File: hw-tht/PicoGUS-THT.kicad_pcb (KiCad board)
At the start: 2 copper layers, 103.7 x 99.8 mm, 82 parts, among them J1 IRQDMA_JP, J3 Bus_ISA_8bit, J5 SJ1-3535NG, J6 UART_TX, J7 USB power jumper, J8 SJ1-3535NG-GR, J9 Waveblaster, U1 Pico, U10 74AHCT126, U11 NE5532, U2 74AHC244, U3 SN74CB3T3257, U4 SN74CB3T3257, U5 74AHC14, U6 74AHC00, U7 74AHC00, U8 APS6404L-3SQR-SN, U9 PCM5100A

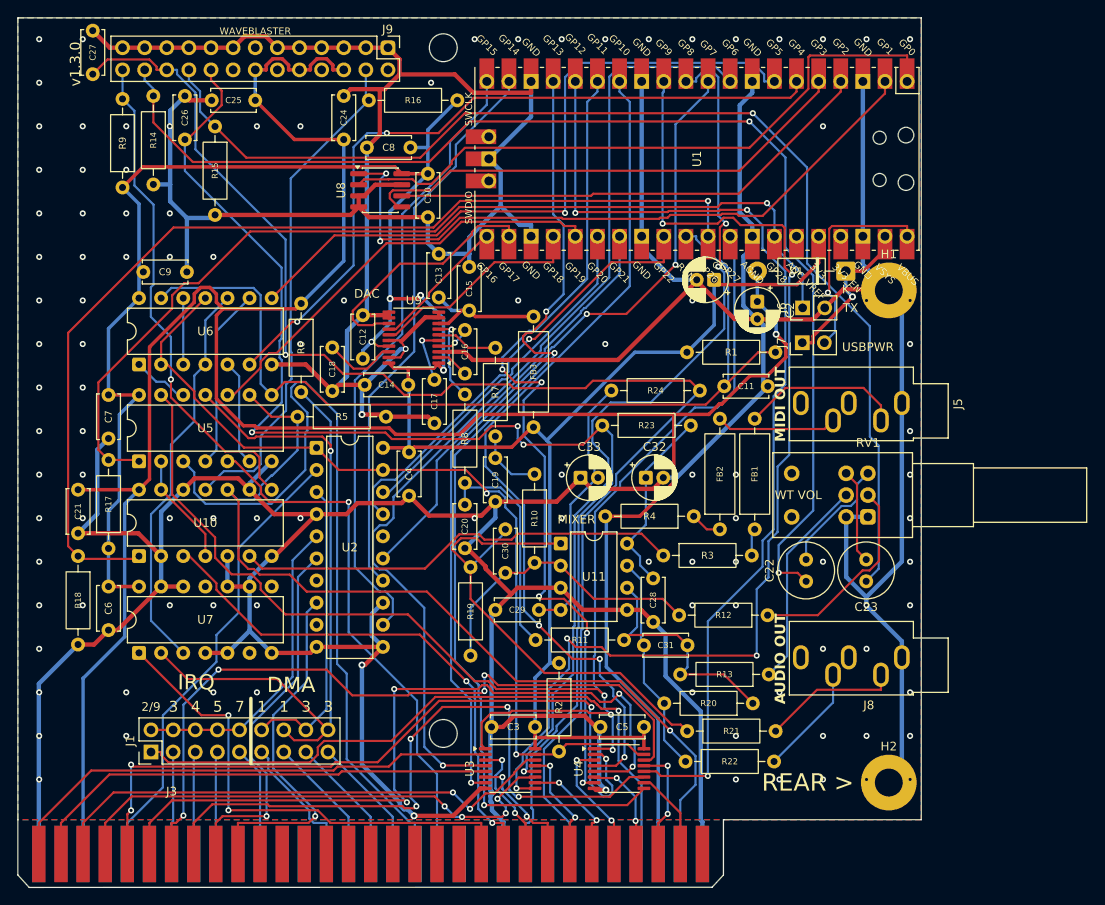
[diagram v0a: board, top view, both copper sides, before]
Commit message: hw-tht: adopt the new hand-made component placement; label clean-up
- THT board rebuilt on the uploaded layout: every part position,
  rotation and reference label kept as placed (R17 moved 0.5 mm down to
  clear C7's courtyard), texts/logo kept; fully re-routed, GND stitched,
  0 DRC errors, 0 unconnected, schematic parity OK. No schematic change
  needed: every cap/resistor sits at the pins it serves.
- Pico pin-name / SWD silkscreen texts removed (THT and SMD).
- WAVEBLASTER, DAC, MIXER and WT VOL labels in Futura bold; WT VOL now
  sits beside RV1 exactly as MIDI OUT / AUDIO OUT sit beside their jacks.
- hw-smd: same label treatment; C23 moved 1.8 mm left to clear WT VOL,
  board re-routed (0 DRC errors).

Co-Authored-By: Claude Opus 5.5 <noreply@anthropic.com>
Claude-Session: https://claude.ai/code/session_011utN3x8yYUNDvkpGCEq5yD
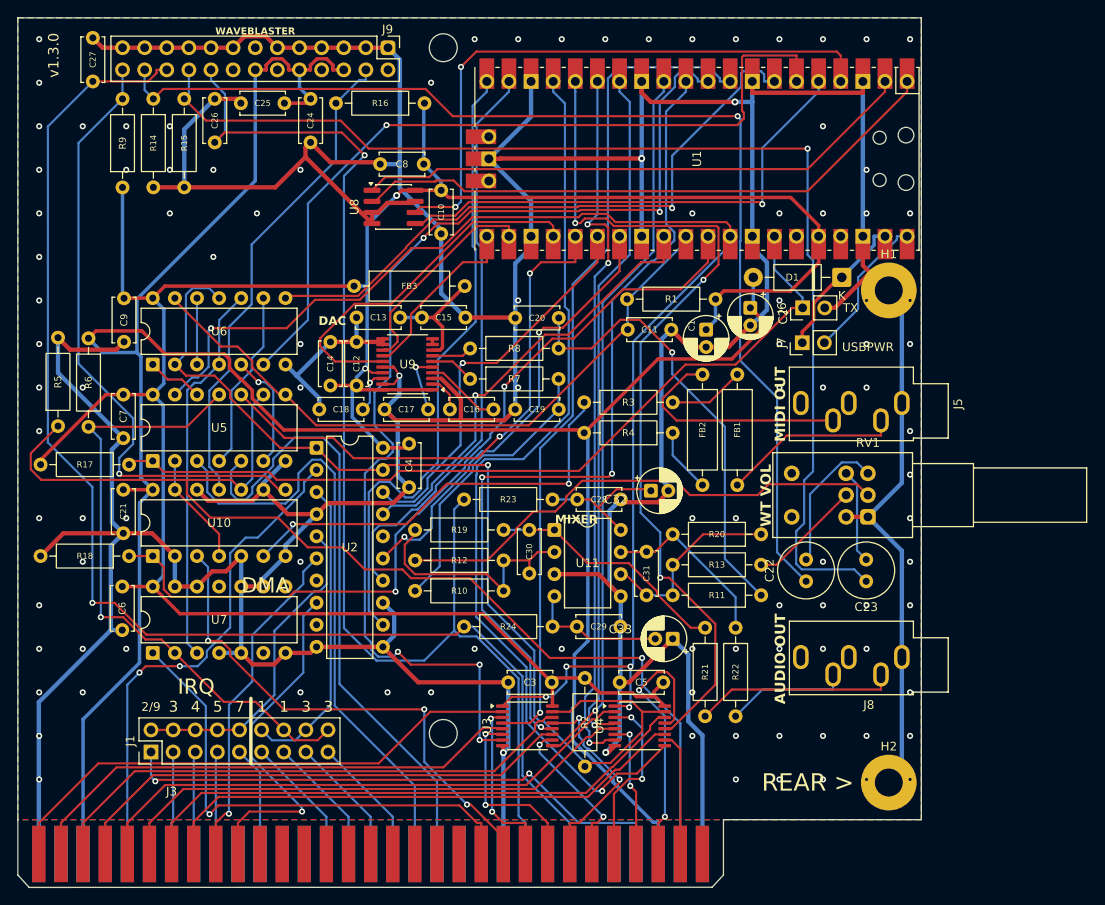
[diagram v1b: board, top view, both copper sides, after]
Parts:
- moved R12 41.0 mm to (162.0, 98.5), turned to 0 degrees
- moved R24 38.3 mm to (167.6, 106.1), turned to 0 degrees
- moved R5 27.5 mm to (121.0, 83.1), turned to 90 degrees
- moved C20 27.1 mm to (173.5, 70.7), turned to 0 degrees
- moved R11 26.4 mm to (201.7, 102.5), turned to 180 degrees
- moved FB3 26.2 mm to (155.0, 67.0), turned to 0 degrees
- moved R6 24.7 mm to (124.5, 73.0)
- moved C33 21.3 mm to (191.6, 107.5), turned to 180 degrees
- moved R3 19.8 mm to (181.4, 80.3)
- moved R20 19.4 mm to (201.7, 95.5)
- moved R10 19.2 mm to (162.0, 102.0), turned to 0 degrees
- moved R23 18.0 mm to (167.6, 91.5)
- moved FB1 17.9 mm to (199.0, 77.2), turned to -90 degrees
- moved R22 16.4 mm to (198.8, 106.2), turned to -90 degrees
- moved R19 15.8 mm to (162.0, 95.0), turned to 0 degrees
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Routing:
- net GND: track 830.6 -> 776.8 mm, vias 109 -> 105
- net AD3: track 126.9 -> 82.1 mm, vias 5 -> 1
- net Net-(R12-Pad1): track 23.5 -> 57.9 mm
- net RUN: track 106.6 -> 77.1 mm
- net Net-(C30-Pad2): track 57.2 -> 28.0 mm
- net AD1: track 98.1 -> 127.0 mm, vias 3 -> 5
- net A5: track 89.0 -> 61.5 mm, vias 4 -> 0
- net /PCM5100 audio/AUDIO_R: track 25.8 -> 51.6 mm, vias 0 -> 1
- net /PCM5100 audio/AUDIO_L: track 7.77 -> 33.2 mm
- net RESET: track 104.0 -> 129.4 mm
- net ~{RI/OCHRDY}: track 117.2 -> 95.5 mm, vias 1 -> 2
- net ~{IOR}: track 90.9 -> 70.6 mm
- net A4: track 84.8 -> 64.8 mm, vias 4 -> 0
- net A6: track 84.6 -> 65.5 mm, vias 4 -> 0
- net AD4: track 97.3 -> 79.0 mm, vias 3 -> 1
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
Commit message: Experimental 2nd IRQ (J10/J11), DMA label fix, labels grouped
- U2's spare channel (2A2 pin 13 -> 2Y2 pin 7, same drive and ~BUSOE as the
  IRQ output) now drives an optional second IRQ: J10 (next to the PSRAM,
  short stub on the fast SPI line) links GPIO3/SPI_TX to 2A2, R25 (10k)
  holds it low when open; J11 (next to J1) links 2Y2 to ISA IRQ3.
  GPIO3 is the PSRAM SPI_TX (all 26 Pico GPIOs are used), so this is for
  firmware that leaves the PSRAM idle. THT and SMD, ERC 0 errors.
- DMA heading moved back beside IRQ above J1.
- Silkscreen labels are members of their circuit-block KiCad groups
  (DAC, MIXER, AUDIO OUT, WT VOL, WAVEBLASTER, MIDI OUT, TX/USBPWR,
  IRQ/DMA + jumper numbers + divider, 2ND IRQ).
- Both boards re-routed: 0 DRC errors, 0 unconnected, schematic parity OK.
- BOMs: R25, J10/J11 (from the 1x40 strip), 6 jumper shunts.

Co-Authored-By: Claude Opus 5.5 <noreply@anthropic.com>
Claude-Session: https://claude.ai/code/session_011utN3x8yYUNDvkpGCEq5yD
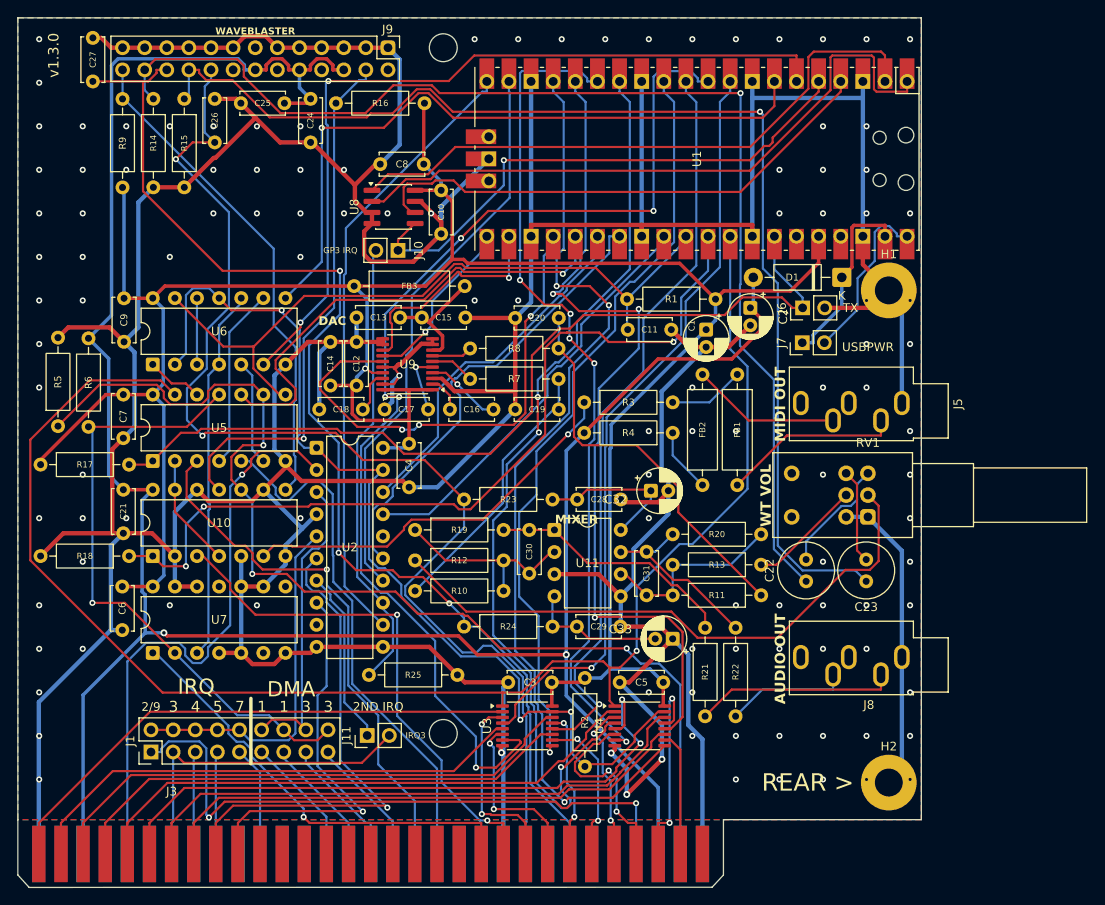
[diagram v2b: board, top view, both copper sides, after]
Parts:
- added J10: Jumper, Connector_PinHeader_2.54mm:PinHeader_1x02_P2.54mm_Vertical, F.Cu at (160.0, 62.9)
- added J11: Jumper, Connector_PinHeader_2.54mm:PinHeader_1x02_P2.54mm_Vertical, F.Cu at (156.5, 118.6)
- added R25: 10K, Resistor_THT:R_Axial_DIN0207_L6.3mm_D2.5mm_P10.16mm_Horizontal, F.Cu at (156.7, 111.7)
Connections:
- U2 pad 13: GND -> IRQ2ND_IN
- U2 pad 7: (no net) -> IRQ2ND_OUT
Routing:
- net IRQ2ND_IN: track 0.00 -> 52.5 mm
- net AD4: track 79.0 -> 108.5 mm, vias 1 -> 3
- net IRQ3: track 11.8 -> 38.4 mm
- net IRQ2ND_OUT: track 0.00 -> 20.2 mm
- net A8: track 39.0 -> 57.6 mm
- net ADS: track 154.9 -> 173.2 mm, vias 5 -> 1
- net -12V: track 149.7 -> 134.1 mm, vias 1 -> 3
- net LRCK: track 42.5 -> 56.9 mm, vias 0 -> 3
- net /Wavetable & line out/~{WT_RESET}: track 71.6 -> 57.2 mm, vias 1 -> 0
- net AD5: track 82.9 -> 96.4 mm, vias 3 -> 5
- net A5: track 61.5 -> 74.2 mm, vias 0 -> 2
- net AD2: track 97.6 -> 85.7 mm, vias 3 -> 1
- net ~{IOW}: track 72.2 -> 60.6 mm
- net Net-(R12-Pad1): track 57.9 -> 68.6 mm
- net +3V3: track 299.1 -> 288.6 mm, vias 2 -> 1
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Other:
- board text added: "2ND IRQ"
- board text added: "GP3 IRQ"
- board text added: "IRQ3"

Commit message: hw-tht: J11 vertical with NE2000/IRQ3 label, H1/H2 silk removed; DigiKey upload CSVs
- J11 stands vertically on J1's pin rows; heading "NE2000 / IRQ3" centred
  above it (replaces "2ND IRQ" + side label); the J11 reference sits beside it.
- H1/H2 reference silkscreen hidden.
- Re-routed (VSYS to J7 hand-routed between the J6 pads on B.Cu):
  0 DRC errors, 0 unconnected, schematic parity OK.
- BOM-*-digikey-upload.csv: quantity, DigiKey PN, MPN and the reference
  designators as Customer Reference (compact ranges, <= 48 chars) so each
  bag is labelled with its board positions.

Co-Authored-By: Claude Opus 5.5 <noreply@anthropic.com>
Claude-Session: https://claude.ai/code/session_011utN3x8yYUNDvkpGCEq5yD
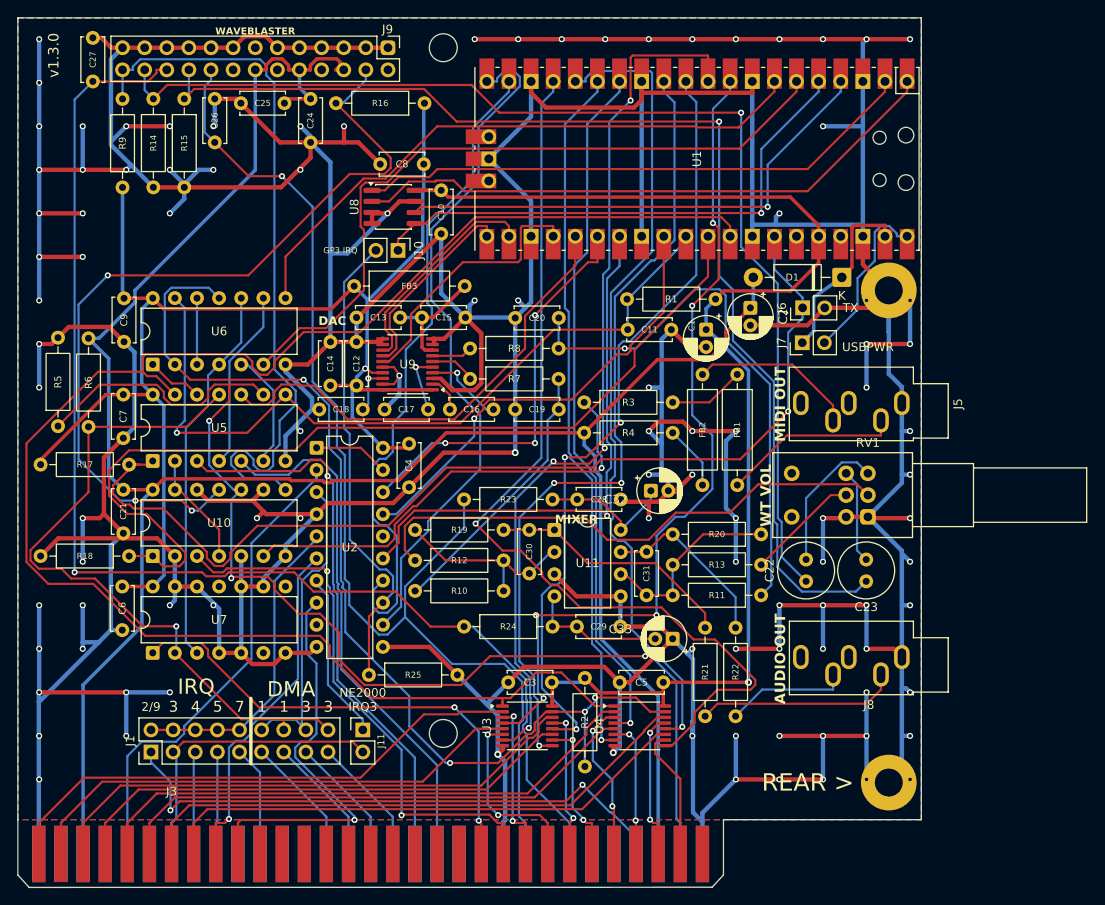
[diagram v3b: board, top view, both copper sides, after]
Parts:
- moved J11 0.81 mm to (156.0, 118.0), turned to 0 degrees
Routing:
- net GND: track 776.2 -> 1165.2 mm, vias 115 -> 102
- net /Wavetable & line out/WT_MIDI: track 61.7 -> 95.4 mm, vias 1 -> 3
- net AD4: track 108.5 -> 80.3 mm, vias 3 -> 1
- net /Wavetable & line out/~{WT_RESET}: track 57.2 -> 84.3 mm
- net AD1: track 128.4 -> 101.8 mm, vias 5 -> 4
- net LRCK: track 56.9 -> 31.1 mm, vias 3 -> 0
- net ADS: track 173.2 -> 194.2 mm, vias 1 -> 0
- net /PCM5100 audio/AUDIO_R: track 45.1 -> 62.9 mm, vias 0 -> 1
- net A8: track 57.6 -> 39.9 mm
- net UART_TX: track 101.5 -> 119.0 mm, vias 0 -> 1
- net AD5: track 96.4 -> 80.4 mm, vias 5 -> 1
- net +3V3: track 288.6 -> 304.3 mm, vias 1 -> 2
- net ~{BUSOE}: track 112.7 -> 128.0 mm, vias 3 -> 4
- net A5: track 74.2 -> 61.5 mm, vias 2 -> 0
- net -12V: track 134.1 -> 146.3 mm, vias 3 -> 1
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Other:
- board text added: "NE2000 IRQ3"
- board text removed: "2ND IRQ"
- board text removed: "IRQ3"

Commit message: v1.3.0: drop the experimental 2nd IRQ; back-side artwork; label clean-up
- Experimental second IRQ removed from both boards: J10, J11 and R25 are gone,
  U2 pin 13 is tied to GND again and pin 7 is unconnected, as on v1.2.
  BOMs and DigiKey upload CSVs: one 10k less, 4 jumper shunts.
- Back silkscreen: the "Mila and Alisa" artwork (hw-common/art/mila-alisa.svg)
  with the dedication below it, mirrored so it reads from the back. On THT it
  is cut out 0.3 mm around every pad and hole, and the dedication sits in the
  one pad-free strip.
- Reference labels: U3/U4 horizontal under the chips; jumper labels J1/J6/J7
  upright; round capacitor labels (C1, C2, C22, C23, C32, C33) moved to free
  spots; the J3 (ISA fingers) label is hidden.
- Both boards: 0 DRC errors, 0 unconnected, schematic parity OK; ERC 0 errors.

Co-Authored-By: Claude Opus 5.5 <noreply@anthropic.com>
Claude-Session: https://claude.ai/code/session_011utN3x8yYUNDvkpGCEq5yD
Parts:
- removed J10, J11: Jumper, Connector_PinHeader_2.54mm:PinHeader_1x02_P2.54mm_Vertical
- removed R25: 10K, Resistor_THT:R_Axial_DIN0207_L6.3mm_D2.5mm_P10.16mm_Horizontal
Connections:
- U2 pad 13: IRQ2ND_IN -> GND
- U2 pad 7: IRQ2ND_OUT -> (no net)
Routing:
- net IRQ2ND_IN: track 54.2 -> 0.00 mm
- net IRQ3: track 34.9 -> 12.1 mm
- net IRQ2ND_OUT: track 19.3 -> 0.00 mm
- net SPI_TX: track 62.0 -> 58.1 mm
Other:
- board text added: "This version is dedicated to Mila and Alisa, my two wonderful princesses, who fill my world with joy."
- board text removed: "GP3 IRQ"
- board text removed: "NE2000 IRQ3"
